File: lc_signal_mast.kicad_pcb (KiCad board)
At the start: 2 copper layers, 28.2 x 98.6 mm, 8 parts, among them J1 Conn_01x04_Male, J2 Conn_01x04_Male

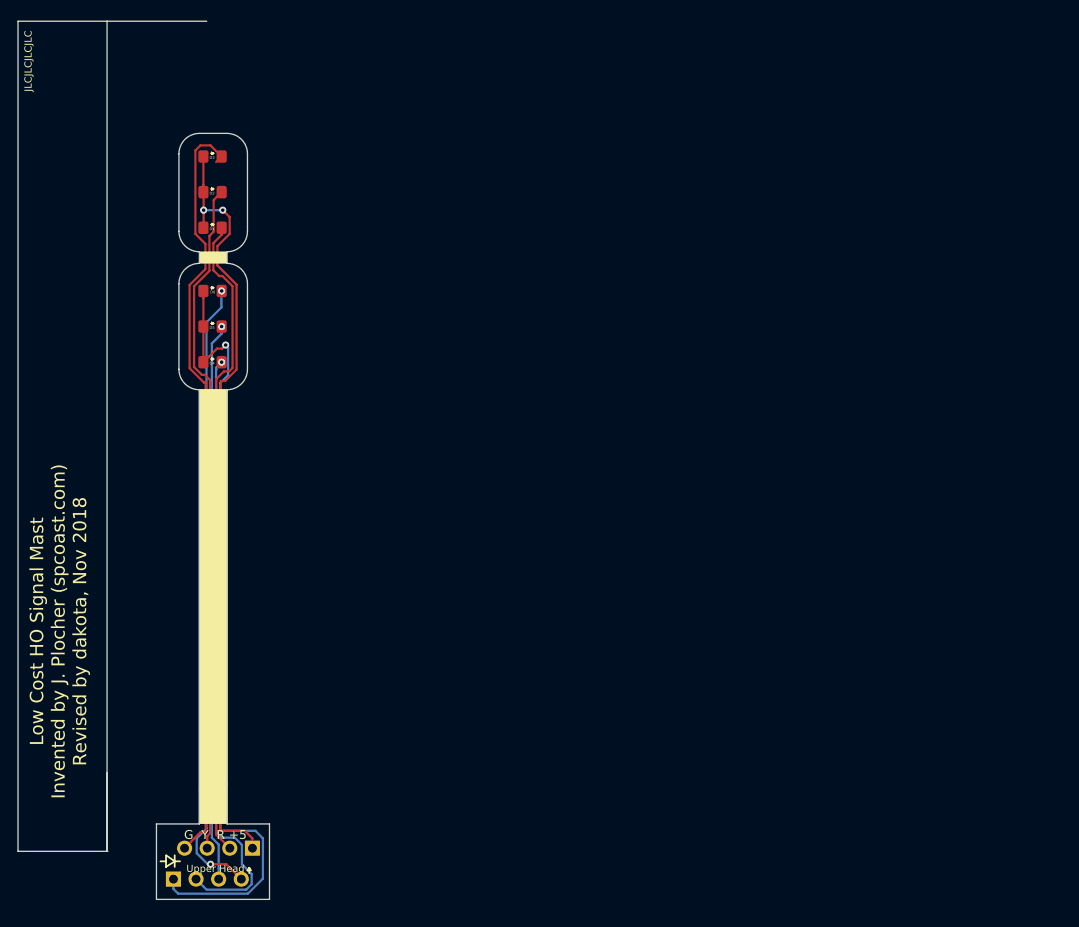
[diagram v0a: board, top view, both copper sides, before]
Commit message: Panelize two-head mast design and clean stuff up.
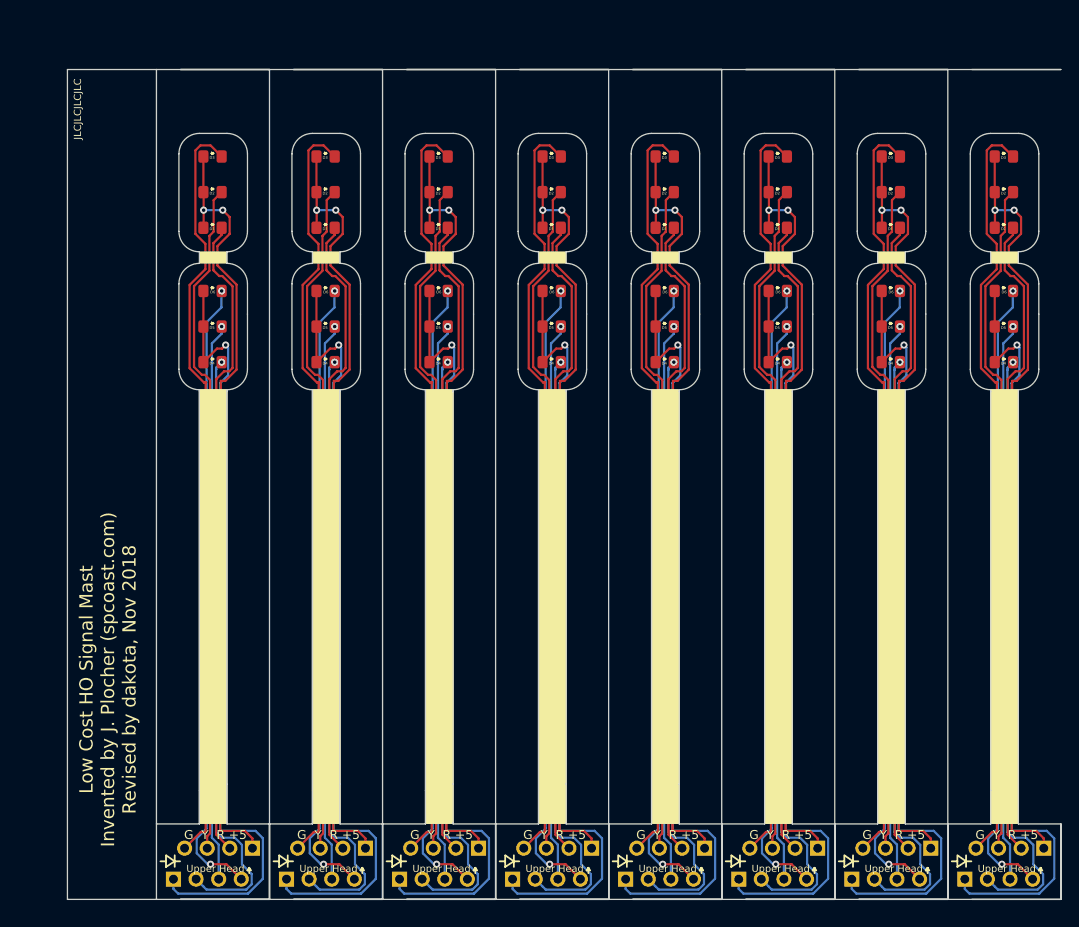
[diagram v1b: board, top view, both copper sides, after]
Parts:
- added D1: LED, dakota_footprints:LED_0805_HandSolder_Pretty, F.Cu at (125.8, 82.2)
- added D1: LED, dakota_footprints:LED_0805_HandSolder_Pretty, F.Cu at (113.1, 82.2)
- added D1: LED, dakota_footprints:LED_0805_HandSolder_Pretty, F.Cu at (100.4, 82.2)
- added D1: LED, dakota_footprints:LED_0805_HandSolder_Pretty, F.Cu at (87.7, 82.2)
- added D1: LED, dakota_footprints:LED_0805_HandSolder_Pretty, F.Cu at (75.0, 82.2)
- added D1: LED, dakota_footprints:LED_0805_HandSolder_Pretty, F.Cu at (62.3, 82.2)
- added D1: LED, dakota_footprints:LED_0805_HandSolder_Pretty, F.Cu at (49.6, 82.2)
- added D2: LED, dakota_footprints:LED_0805_HandSolder_Pretty, F.Cu at (125.8, 78.2)
- added D2: LED, dakota_footprints:LED_0805_HandSolder_Pretty, F.Cu at (113.1, 78.2)
- added D2: LED, dakota_footprints:LED_0805_HandSolder_Pretty, F.Cu at (100.4, 78.2)
- added D2: LED, dakota_footprints:LED_0805_HandSolder_Pretty, F.Cu at (87.7, 78.2)
- added D2: LED, dakota_footprints:LED_0805_HandSolder_Pretty, F.Cu at (75.0, 78.2)
- added D2: LED, dakota_footprints:LED_0805_HandSolder_Pretty, F.Cu at (62.3, 78.2)
- added D2: LED, dakota_footprints:LED_0805_HandSolder_Pretty, F.Cu at (49.6, 78.2)
- added D3: LED, dakota_footprints:LED_0805_HandSolder_Pretty, F.Cu at (125.8, 74.2)
- added D3: LED, dakota_footprints:LED_0805_HandSolder_Pretty, F.Cu at (113.1, 74.2)
- added D3: LED, dakota_footprints:LED_0805_HandSolder_Pretty, F.Cu at (100.4, 74.2)
- added D3: LED, dakota_footprints:LED_0805_HandSolder_Pretty, F.Cu at (87.7, 74.2)
- added D3: LED, dakota_footprints:LED_0805_HandSolder_Pretty, F.Cu at (75.0, 74.2)
- added D3: LED, dakota_footprints:LED_0805_HandSolder_Pretty, F.Cu at (62.3, 74.2)
- added D3: LED, dakota_footprints:LED_0805_HandSolder_Pretty, F.Cu at (49.6, 74.2)
- added D4: LED, dakota_footprints:LED_0805_HandSolder_Pretty, F.Cu at (125.8, 97.3)
- added D4: LED, dakota_footprints:LED_0805_HandSolder_Pretty, F.Cu at (113.1, 97.3)
- added D4: LED, dakota_footprints:LED_0805_HandSolder_Pretty, F.Cu at (100.4, 97.3)
- added D4: LED, dakota_footprints:LED_0805_HandSolder_Pretty, F.Cu at (87.7, 97.3)
- added D4: LED, dakota_footprints:LED_0805_HandSolder_Pretty, F.Cu at (75.0, 97.3)
- added D4: LED, dakota_footprints:LED_0805_HandSolder_Pretty, F.Cu at (62.3, 97.3)
- added D4: LED, dakota_footprints:LED_0805_HandSolder_Pretty, F.Cu at (49.6, 97.3)
- added D5: LED, dakota_footprints:LED_0805_HandSolder_Pretty, F.Cu at (125.8, 93.3)
- added D5: LED, dakota_footprints:LED_0805_HandSolder_Pretty, F.Cu at (113.1, 93.3)
- added D5: LED, dakota_footprints:LED_0805_HandSolder_Pretty, F.Cu at (100.4, 93.3)
- added D5: LED, dakota_footprints:LED_0805_HandSolder_Pretty, F.Cu at (87.7, 93.3)
- added D5: LED, dakota_footprints:LED_0805_HandSolder_Pretty, F.Cu at (75.0, 93.3)
- added D5: LED, dakota_footprints:LED_0805_HandSolder_Pretty, F.Cu at (62.3, 93.3)
- added D5: LED, dakota_footprints:LED_0805_HandSolder_Pretty, F.Cu at (49.6, 93.3)
- added D6: LED, dakota_footprints:LED_0805_HandSolder_Pretty, F.Cu at (125.8, 89.3)
- added D6: LED, dakota_footprints:LED_0805_HandSolder_Pretty, F.Cu at (113.1, 89.3)
- added D6: LED, dakota_footprints:LED_0805_HandSolder_Pretty, F.Cu at (100.4, 89.3)
- added D6: LED, dakota_footprints:LED_0805_HandSolder_Pretty, F.Cu at (87.7, 89.3)
- added D6: LED, dakota_footprints:LED_0805_HandSolder_Pretty, F.Cu at (75.0, 89.3)
- added D6: LED, dakota_footprints:LED_0805_HandSolder_Pretty, F.Cu at (62.3, 89.3)
- added D6: LED, dakota_footprints:LED_0805_HandSolder_Pretty, F.Cu at (49.6, 89.3)
- added J1: Conn_01x04_Male, dakota_footprints:PinHeader_1x04_P2.54mm_Horizontal_Unmarked, F.Cu at (130.3, 151.9)
- added J1: Conn_01x04_Male, dakota_footprints:PinHeader_1x04_P2.54mm_Horizontal_Unmarked, F.Cu at (117.6, 151.9)
- added J1: Conn_01x04_Male, dakota_footprints:PinHeader_1x04_P2.54mm_Horizontal_Unmarked, F.Cu at (104.9, 151.9)
- added J1: Conn_01x04_Male, dakota_footprints:PinHeader_1x04_P2.54mm_Horizontal_Unmarked, F.Cu at (92.2, 151.9)
- added J1: Conn_01x04_Male, dakota_footprints:PinHeader_1x04_P2.54mm_Horizontal_Unmarked, F.Cu at (79.5, 151.9)
- added J1: Conn_01x04_Male, dakota_footprints:PinHeader_1x04_P2.54mm_Horizontal_Unmarked, F.Cu at (66.8, 151.9)
- added J1: Conn_01x04_Male, dakota_footprints:PinHeader_1x04_P2.54mm_Horizontal_Unmarked, F.Cu at (54.1, 151.9)
- added J2: Conn_01x04_Male, dakota_footprints:PinHeader_1x04_P2.54mm_Horizontal_Unmarked, B.Cu at (121.4, 155.4)
- added J2: Conn_01x04_Male, dakota_footprints:PinHeader_1x04_P2.54mm_Horizontal_Unmarked, B.Cu at (108.7, 155.4)
- added J2: Conn_01x04_Male, dakota_footprints:PinHeader_1x04_P2.54mm_Horizontal_Unmarked, B.Cu at (96.0, 155.4)
- added J2: Conn_01x04_Male, dakota_footprints:PinHeader_1x04_P2.54mm_Horizontal_Unmarked, B.Cu at (83.3, 155.4)
- added J2: Conn_01x04_Male, dakota_footprints:PinHeader_1x04_P2.54mm_Horizontal_Unmarked, B.Cu at (70.6, 155.4)
- added J2: Conn_01x04_Male, dakota_footprints:PinHeader_1x04_P2.54mm_Horizontal_Unmarked, B.Cu at (57.9, 155.4)
- added J2: Conn_01x04_Male, dakota_footprints:PinHeader_1x04_P2.54mm_Horizontal_Unmarked, B.Cu at (45.2, 155.4)
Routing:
- net /+5V_2: track 88.1 -> 705.1 mm, vias 1 -> 8
- net /+5V_1: track 87.8 -> 702.3 mm, vias 2 -> 16
- net /GREEN1: track 86.4 -> 684.1 mm
- net /YELLOW1: track 76.1 -> 608.5 mm
- net /RED1: track 72.9 -> 583.2 mm
- net /GREEN2: track 70.7 -> 566.0 mm, vias 2 -> 16
- net /RED2: track 69.0 -> 552.1 mm, vias 1 -> 8
- net /YELLOW2: track 63.5 -> 507.7 mm, vias 1 -> 8
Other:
- board size 28.2 x 98.6 mm -> 111.6 x 93.2 mm

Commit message: More small fixes
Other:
- board text added: "Low Cost HO Signal Mast v2 Invented by J. Plocher (spcoast.com) Revised by dakota, Dec 2018"
- board text removed: "Low Cost HO Signal Mast Invented by J. Plocher (spcoast.com) Revised by dakota, Nov 2018"
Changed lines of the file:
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@@
   (general
     (thickness 1.6)
-    (drawings 564)
+    (drawings 565)
     (tracks 936)
     (zones 0)
@@
     (35 F.Paste user)
     (36 B.SilkS user)
-    (37 F.SilkS user hide)
+    (37 F.SilkS user)
     (38 B.Mask user)
     (39 F.Mask user)
@@
     )
   )
+  (gr_line (start 132.2 64.475) (end 132.2 149.225) (layer Edge.Cuts) (width 0.0254))
   (gr_text "G  Y  R +5" (at 125.55 153.725) (layer B.SilkS)
     (effects (font (size 1 1) (thickness 0.25)) (justify mirror))
@@
   (gr_line (start 43.3 157.7) (end 30.6 157.7) (layer Edge.Cuts) (width 0.0254))
   (gr_line (start 43.3 149.225) (end 43.3 157.7) (layer Edge.Cuts) (width 0.0254))
-  (gr_text "Low Cost HO Signal Mast\nInvented by J. Plocher (spcoast.com)\nRevised by dakota, Nov 2018" (at 25.15 133 90) (layer F.SilkS)
+  (gr_text "Low Cost HO Signal Mast v2\nInvented by J. Plocher (spcoast.com)\nRevised by dakota, Dec 2018" (at 25.15 133 90) (layer F.SilkS)
     (effects (font (size 1.5 1.5) (thickness 0.3)))
   )
